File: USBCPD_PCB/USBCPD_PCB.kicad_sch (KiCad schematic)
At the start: 0 parts

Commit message: Added new Parts
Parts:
- added IC1: TMCS1108A3BQDRQ1, SOIC127P600X175-8N, symbol SamacSys_Parts:TMCS1108A3BQDRQ1
- added IC2, IC3: UCC27282QDRQ1, SOIC127P600X175-8N, symbol SamacSys_Parts:UCC27282QDRQ1
- added Q1, Q2, Q3, Q4: SIR584DP-T1-RE3, SIR582DPT1RE3, symbol SamacSys_Parts:SIR584DP-T1-RE3
- added U1: NUCLEO-G474RE, USBC_PD:ST_NUCLEO-G474RE, symbol USBC_PD:NUCLEO-G474RE

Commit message: new components added
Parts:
- added C?: A768MS277M1VLAS022, CAPAE1030X1270N, symbol SamacSys_Parts:A768MS277M1VLAS022
- added C? (x4): GRM32DL8EL475KE07K, CAPC3225X220N, symbol SamacSys_Parts:GRM32DL8EL475KE07K
- added C?: EEE-TP1K391M, EEEFK0J682AM, symbol SamacSys_Parts:EEE-TP1K391M
- added L?: SRP1038WA-150M, SRP1038WA150M, symbol SamacSys_Parts:SRP1038WA-150M
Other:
- moved on the sheet: IC1, IC2, IC3, Q1, Q2, Q3, Q4

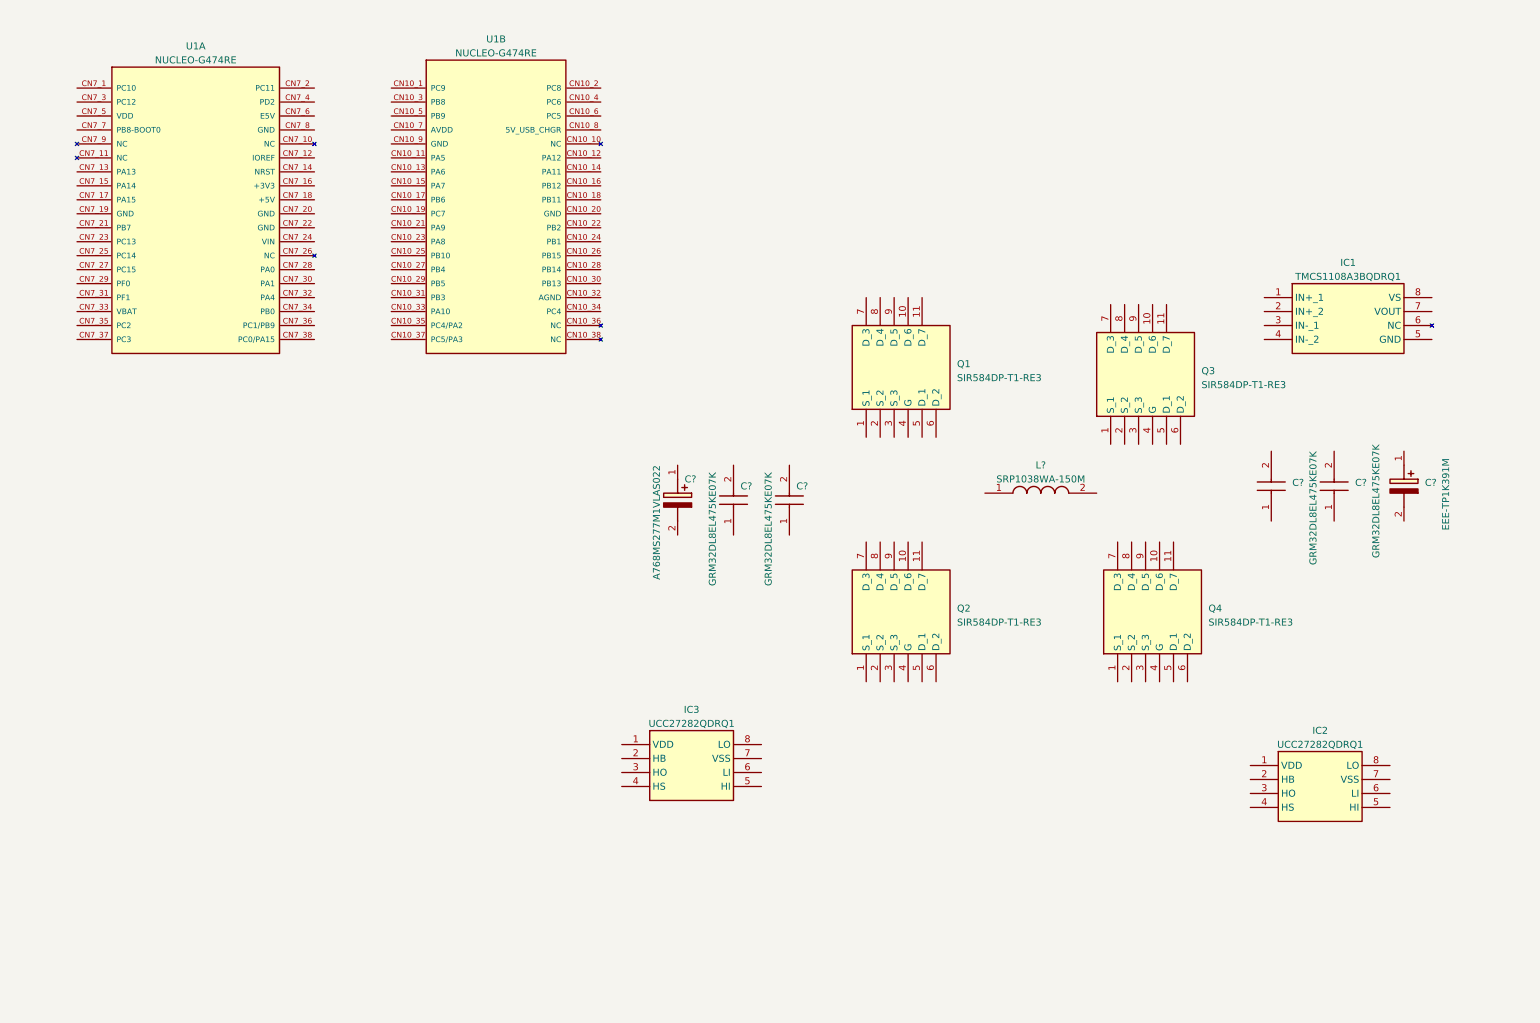
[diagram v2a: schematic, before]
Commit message: added resistors, tvs and voltage control
also wired up first changes
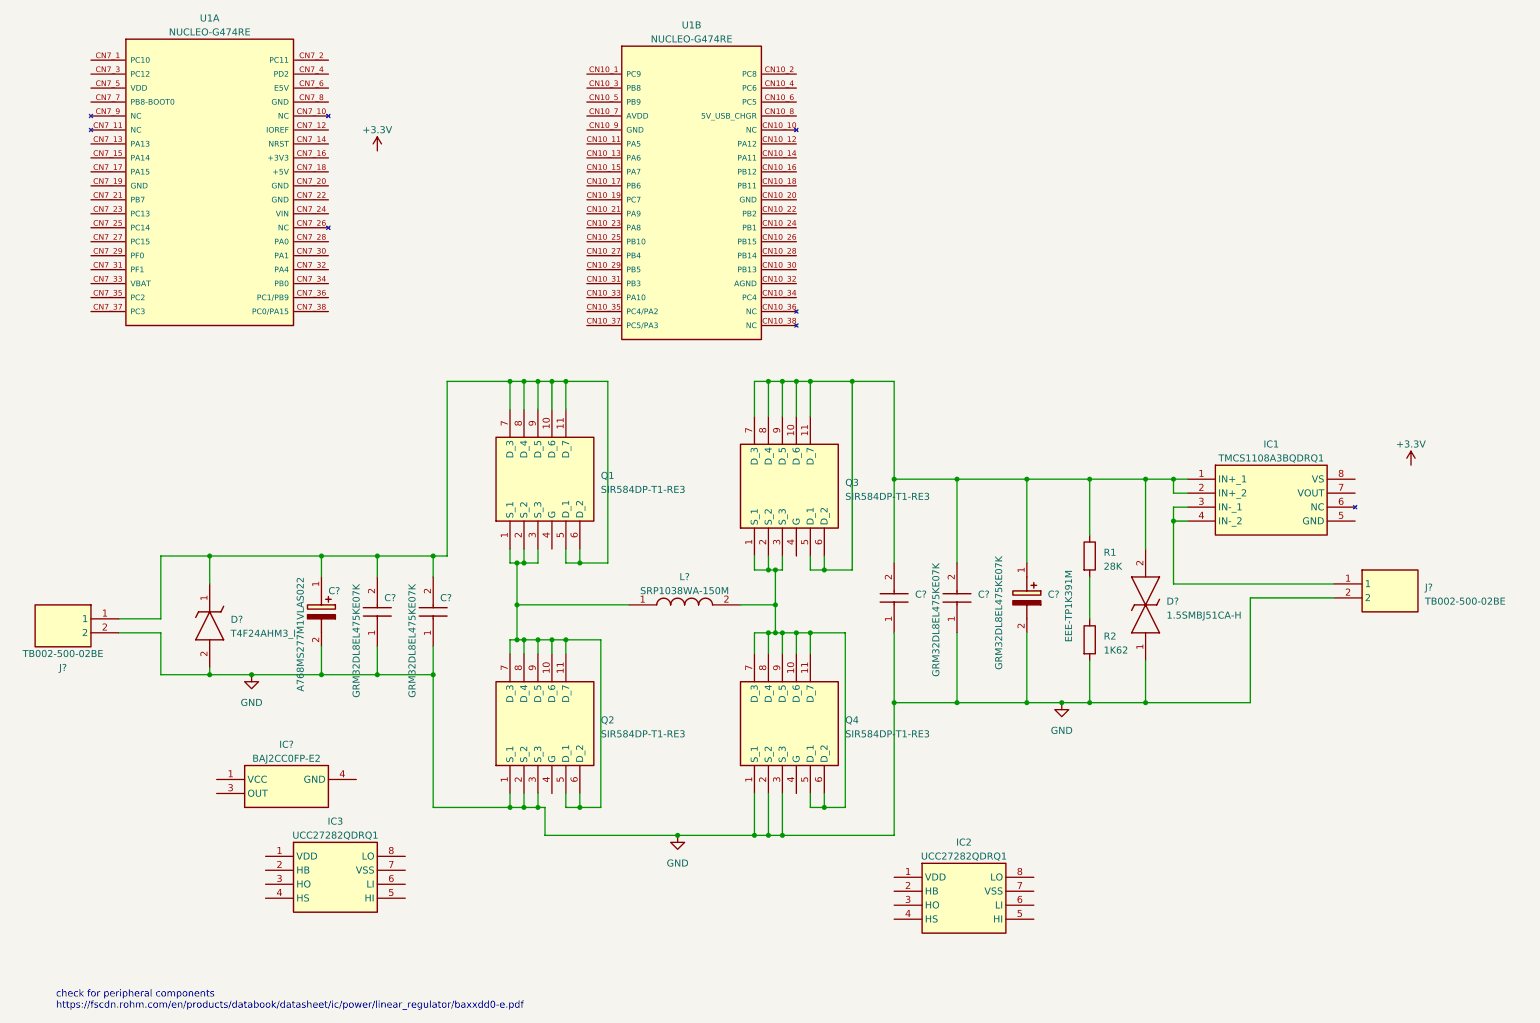
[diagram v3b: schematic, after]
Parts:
- added D?: 1.5SMBJ51CA-H, DIONM5436X244N, symbol SamacSys_Parts:1.5SMBJ51CA-H
- added D?: T4F24AHM3_I, SODFL3718X108N, symbol SamacSys_Parts:T4F24AHM3_I
- added IC?: BAJ2CC0FP-E2, BD750L5FPCE2, symbol SamacSys_Parts:BAJ2CC0FP-E2
- added J? (x2): TB002-500-02BE, TB00250002BE, symbol SamacSys_Parts:TB002-500-02BE
- added R1: 28K, Resistor_SMD:R_0603_1608Metric_Pad0.98x0.95mm_HandSolder, symbol Device:R
- added R2: 1K62, Resistor_SMD:R_0603_1608Metric_Pad0.98x0.95mm_HandSolder, symbol Device:R
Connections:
- net at L?.1: now also Q1.1 (S_1), Q1.2 (S_2), Q1.3 (S_3), Q2.10 (D_6), Q2.11 (D_7), Q2.5 (D_1), Q2.6 (D_2), Q2.7 (D_3), Q2.8 (D_4), Q2.9 (D_5)
- net at L?.2: now also Q3.1 (S_1), Q3.2 (S_2), Q3.3 (S_3), Q4.10 (D_6), Q4.11 (D_7), Q4.5 (D_1), Q4.6 (D_2), Q4.7 (D_3), Q4.8 (D_4), Q4.9 (D_5)
- net GND: now reaches Q2.1 (S_1)
- net GND: now also C?.1, C?.1, C?.1, C?.1, C?.2 (-), C?.2 (-), Q2.2 (S_2), Q2.3 (S_3), Q4.1 (S_1), Q4.2 (S_2), Q4.3 (S_3), D?.1, D?.2 (A), J?.2, J?.2, R2.2
- net at C?.1 (+): now also C?.2, C?.2, Q1.10 (D_6), Q1.11 (D_7), Q1.5 (D_1), Q1.6 (D_2), Q1.7 (D_3), Q1.8 (D_4), Q1.9 (D_5), D?.1 (K), J?.1
- net at Q3.10 (D_6): now also C?.1 (+), C?.2, C?.2, IC1.1 (IN+_1), IC1.2 (IN+_2), Q3.11 (D_7), Q3.5 (D_1), Q3.6 (D_2), Q3.7 (D_3), Q3.8 (D_4), Q3.9 (D_5), D?.2, R1.1
- net at IC1.3 (IN-_1): now also IC1.4 (IN-_2), J?.1
- new net: R1.2, R2.1
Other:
- note added: "check for peripheral components https://fscdn.rohm.com/en/products/databook/datasheet/ic/power/linear_regulator/baxxdd0-e.pdf"
- moved on the sheet: C?, IC1, IC2, IC3, L?, Q1, Q2, Q3, Q4, U1A, U1B

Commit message: added additional components
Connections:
- net +3.3V: now also IC1.8 (VS)
- net GND: now also IC1.5 (GND)
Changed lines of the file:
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@@
+    (stroke (width 0) (type default))
+  )
+  (wire (pts (xy 255.27 105.41) (xy 255.27 102.87))
     (stroke (width 0) (type default))
   )
@@
     (stroke (width 0) (type default))
   )
+  (wire (pts (xy 262.89 95.25) (xy 262.89 92.71))
+    (stroke (width 0) (type default))
+  )
   (wire (pts (xy 214.63 135.89) (xy 204.47 135.89))
     (stroke (width 0) (type default))
@@
     (stroke (width 0) (type default))
   )
+  (wire (pts (xy 255.27 102.87) (xy 252.73 102.87))
+    (stroke (width 0) (type default))
+  )
   (wire (pts (xy 111.76 154.94) (xy 115.57 154.94))
     (stroke (width 0) (type default))
@@
   )
   (wire (pts (xy 146.05 109.22) (xy 146.05 111.76))
+    (stroke (width 0) (type default))
+  )
+  (wire (pts (xy 252.73 95.25) (xy 262.89 95.25))
     (stroke (width 0) (type default))
   )
@@
         )
       )
+    )
+  )
+  (symbol (lib_id "power:GND") (at 255.27 105.41 0) (unit 1)
+    (in_bom yes) (on_board yes) (dnp no) (fields_autoplaced)
+    (property "Reference" "#PWR06" (at 255.27 111.76 0)
+      (effects (font (size 1.27 1.27)) hide)
+    )
+    (property "Value" "GND" (at 255.27 110.49 0)
+      (effects (font (size 1.27 1.27)))
+    )
+    (property "Footprint" "" (at 255.27 105.41 0)
+      (effects (font (size 1.27 1.27)) hide)
+    )
+    (property "Datasheet" "" (at 255.27 105.41 0)
+      (effects (font (size 1.27 1.27)) hide)
+    )
+    (pin "1")
+    (instances
+      (project "USBCPD_PCB"
+        (path "/d348c750-b8a4-4ea0-a85d-ac4257fd8477"
+          (reference "#PWR06") (unit 1)
+        )
+      )

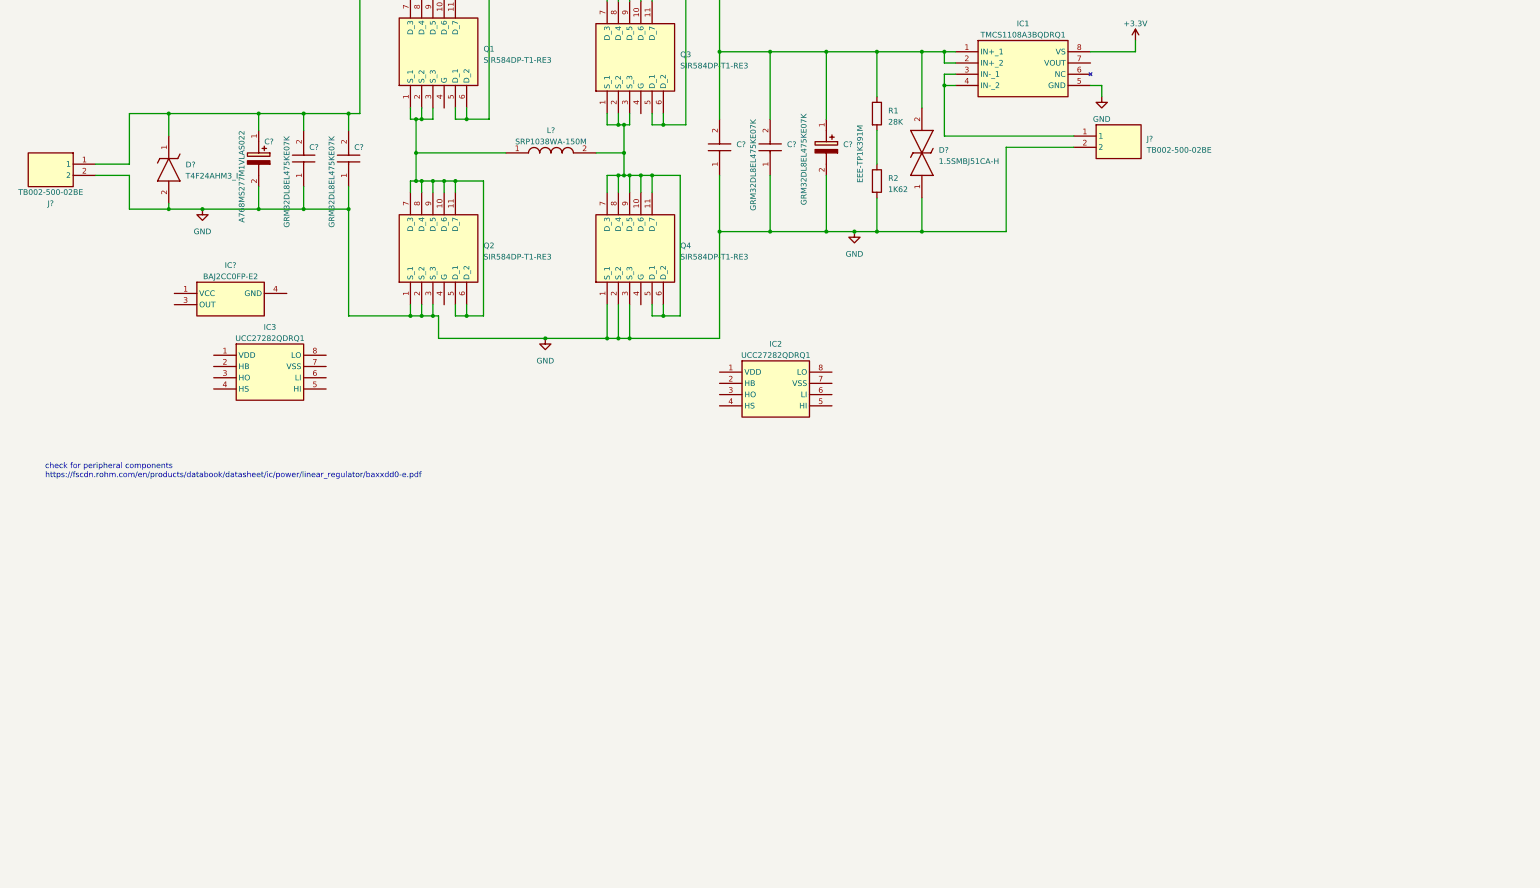
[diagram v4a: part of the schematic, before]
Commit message: Added Gate Driver Circuitry
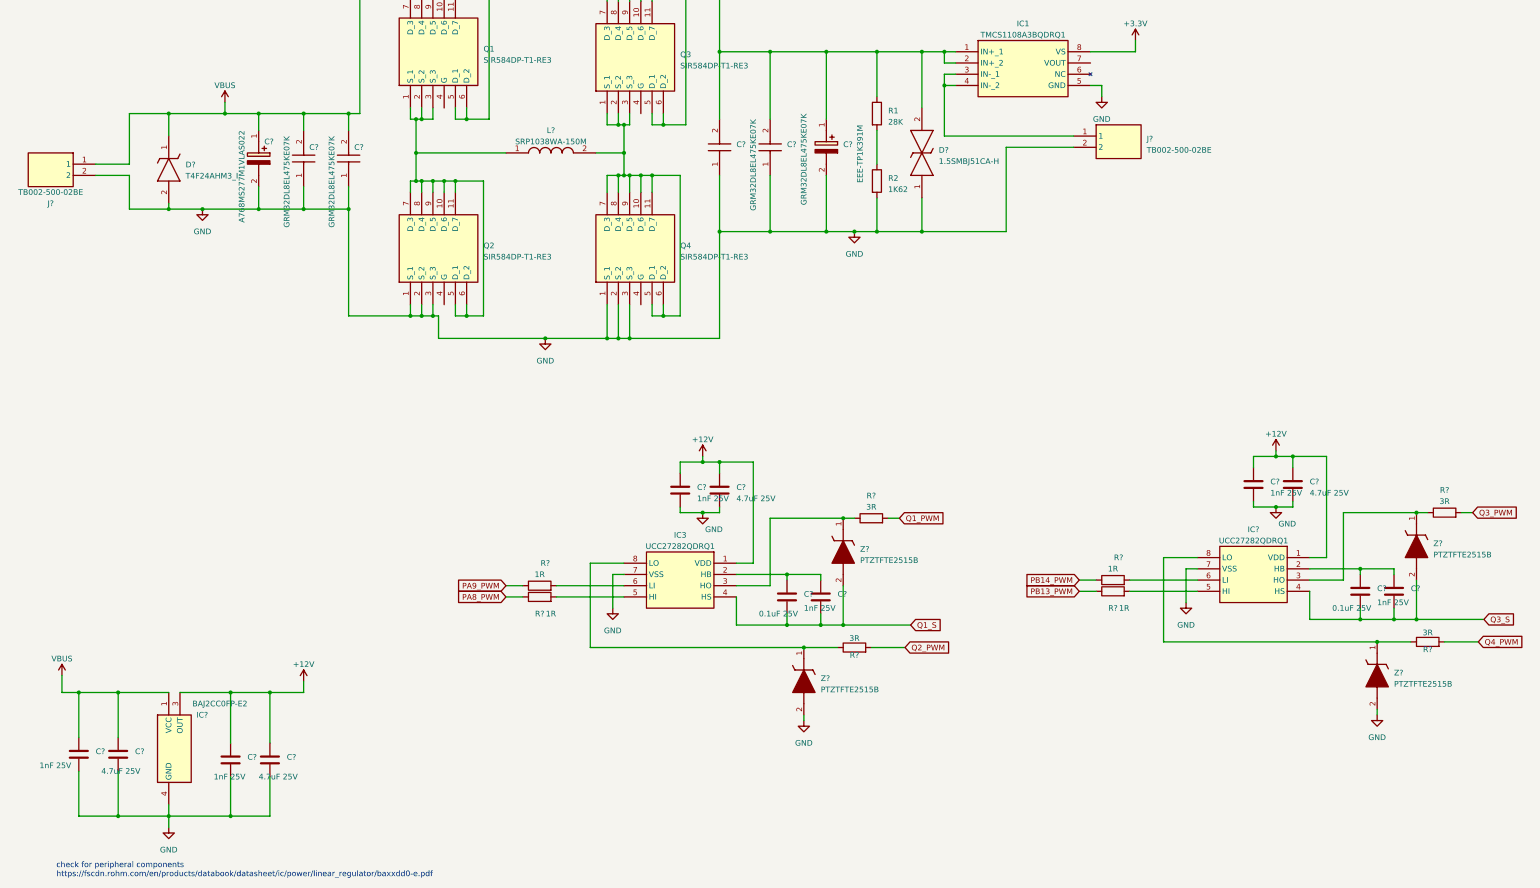
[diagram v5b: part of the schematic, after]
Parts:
- removed IC2: UCC27282QDRQ1, SOIC127P600X175-8N, symbol SamacSys_Parts:UCC27282QDRQ1
- added C? (x4): 4.7uF 25V, Capacitor_SMD:C_0603_1608Metric_Pad1.08x0.95mm_HandSolder, symbol Device:C
- added C? (x6): 1nF 25V, Capacitor_SMD:C_0402_1005Metric_Pad0.74x0.62mm_HandSolder, symbol Device:C
- added C? (x2): 0.1uF 25V, Capacitor_SMD:C_0603_1608Metric_Pad1.08x0.95mm_HandSolder, symbol Device:C
- added IC?: UCC27282QDRQ1, SOIC127P600X175-8N, symbol SamacSys_Parts:UCC27282QDRQ1
- added R? (x4): 1R, Resistor_SMD:R_0603_1608Metric_Pad0.98x0.95mm_HandSolder, symbol Device:R
- added R? (x4): 3R, Resistor_SMD:R_0603_1608Metric_Pad0.98x0.95mm_HandSolder, symbol Device:R
- added Z? (x4): PTZTFTE2515B, PTZTFTE2515B, symbol SamacSys_Parts:PTZTFTE2515B
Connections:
- net GND: now also IC3.7 (VSS), IC?.4 (GND), C?.2, C?.2, C?.2, C?.2, C?.2, C?.2, C?.2, C?.2, IC?.7 (VSS), Z?.2 (A), Z?.2 (A)
- net VBUS: now reaches IC?.1 (VCC)
- net VBUS: now also C?.1 (+), C?.2, C?.2, D?.1 (K), J?.1, Q1.10 (D_6), Q1.11 (D_7), Q1.5 (D_1), Q1.6 (D_2), Q1.7 (D_3), Q1.8 (D_4), Q1.9 (D_5), C?.1, C?.1
- net +12V: now reaches IC?.3 (OUT)
- net +12V: now also IC3.1 (VDD), C?.1, C?.1, C?.1, C?.1, C?.1, C?.1, IC?.1 (VDD)
- net at IC3.2 (HB): now also C?.1, C?.2
- net at IC3.3 (HO): now also R?.1, Z?.1 (K)
- net Q1_S: now reaches IC3.4 (HS)
- net Q1_S: now also C?.1, C?.2, Z?.2 (A)
- net at IC3.5 (HI): now also R?.2
- net at IC3.6 (LI): now also R?.2
- net at IC3.8 (LO): now also R?.1, Z?.1 (K)
- new net: C?.1, C?.2, IC?.2 (HB)
- new net: IC?.3 (HO), R?.1, Z?.1 (K)
- new net: IC?.5 (HI), R?.2
- new net: IC?.6 (LI), R?.2
- new net: IC?.8 (LO), R?.1, Z?.1 (K)
- new net PA8_PWM: R?.1
- new net PA9_PWM: R?.1
- new net PB13_PWM: R?.1
- new net PB14_PWM: R?.1
- new net Q1_PWM: R?.2
- new net Q2_PWM: R?.2
- new net Q3_PWM: R?.2
- new net Q3_S: C?.1, C?.2, IC?.4 (HS), Z?.2 (A)
- new net Q4_PWM: R?.2
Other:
- moved on the sheet: IC3, IC?

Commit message: finished up main schematic
finalized wiring, added leds with resistors, fixed ERC errors
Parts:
- removed C? (x2): 4.7uF 25V, Capacitor_SMD:C_0603_1608Metric_Pad1.08x0.95mm_HandSolder, symbol Device:C
- removed R1: 28K, Resistor_SMD:R_0603_1608Metric_Pad0.98x0.95mm_HandSolder, symbol Device:R
- removed R2: 1K62, Resistor_SMD:R_0603_1608Metric_Pad0.98x0.95mm_HandSolder, symbol Device:R
- added JP1: SolderJumper_2_Bridged, Jumper:SolderJumper-2_P1.3mm_Bridged_RoundedPad1.0x1.5mm, symbol Jumper:SolderJumper_2_Bridged
- added LED1: 150060BS75003, 150060BS75003, symbol SamacSys_Parts:150060BS75003
- added LED2: 150060GS75003, LEDC1608X80N, symbol SamacSys_Parts:150060GS75003
- added LED3: 150060SS75003, 150060SS75003, symbol SamacSys_Parts:150060SS75003
- added R10: 2.8K, Resistor_SMD:R_0603_1608Metric_Pad0.98x0.95mm_HandSolder, symbol Device:R
- added R11, R8: 100R, Resistor_SMD:R_0603_1608Metric_Pad0.98x0.95mm_HandSolder, symbol Device:R
- added R13: 28K, Resistor_SMD:R_0603_1608Metric_Pad0.98x0.95mm_HandSolder, symbol Device:R
- added R14: 1K62, Resistor_SMD:R_0603_1608Metric_Pad0.98x0.95mm_HandSolder, symbol Device:R
- added R5: 1R, Resistor_SMD:R_0603_1608Metric_Pad0.98x0.95mm_HandSolder, symbol Device:R
- added R9: 900R, Resistor_SMD:R_0603_1608Metric_Pad0.98x0.95mm_HandSolder, symbol Device:R
- added S1: EVP-BDCC1A000, EVPBDCC1A000, symbol SamacSys_Parts:EVP-BDCC1A000
- added TP1, TP10, TP2, TP3, TP4, TP5, TP6, TP7, TP8, TP9: TestPoint, TestPoint:TestPoint_THTPad_2.0x2.0mm_Drill1.0mm, symbol Connector:TestPoint
- added unit 5 of U1
- added unit 4 of U1
- added unit 3 of U1
- added unit 6 of U1
- C1: renamed from C?; value 1nF 25V -> 1uF 25V; footprint Capacitor_SMD:C_0402_1005Metric_Pad0.74x0.62mm_HandSolder -> Capacitor_SMD:C_0603_1608Metric_Pad1.08x0.95mm_HandSolder
- C4: renamed from C?; value 1nF 25V -> 0.33uF 25V; footprint Capacitor_SMD:C_0402_1005Metric_Pad0.74x0.62mm_HandSolder -> Capacitor_SMD:C_0603_1608Metric_Pad1.08x0.95mm_HandSolder
- Q1, Q2, Q3, Q4: footprint SIR582DPT1RE3 -> SamacSys_Parts:SIR584DPT1RE3
- gave numbers to parts that had none: 33
- renumbered IC3 to IC2
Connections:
- net +12V: now also TP1.1
- net +3.3V: now also U1.CN7_16 (+3V3)
- net GND: now also U1.CN7_20 (GND), U1.CN7_22 (GND), U1.CN7_8 (GND), JP1.1 (A), LED1.2 (K), LED2.1 (K), LED3.1 (K), R14.2, R8.2
- net PA8_PWM: now also U1.CN10_23 (PA8)
- net PA9_PWM: now also U1.CN10_21 (PA9)
- net PB13_PWM: now also U1.CN10_30 (PB13)
- net PB14_PWM: now also U1.CN10_28 (PB14)
- net Q1_PWM: now also Q1.4 (G)
- net Q1_S: now also L1.1, Q1.1 (S_1), Q1.2 (S_2), Q1.3 (S_3), Q2.10 (D_6), Q2.11 (D_7), Q2.5 (D_1), Q2.6 (D_2), Q2.7 (D_3), Q2.8 (D_4), Q2.9 (D_5), TP3.1
- net Q2_PWM: now also Q2.4 (G)
- net Q3_PWM: now also Q3.4 (G)
- net Q3_S: now also L1.2, Q3.1 (S_1), Q3.2 (S_2), Q3.3 (S_3), Q4.10 (D_6), Q4.11 (D_7), Q4.5 (D_1), Q4.6 (D_2), Q4.7 (D_3), Q4.8 (D_4), Q4.9 (D_5), TP4.1
- net Q4_PWM: now also Q4.4 (G)
- net VBUS: now also R9.1, TP2.1
- net at IC3.3 (HO), R15.1, Z4.1 (K): now also TP10.1
- net at IC3.8 (LO), R12.1, Z3.1 (K): now also TP9.1
- net at IC2.3 (HO), R4.1, Z2.1 (K): now also TP7.1
- net at IC1.3 (IN-_1), IC1.4 (IN-_2), J2.1: now also TP8.1
- net at IC2.8 (LO), R3.1, Z1.1 (K): now also TP6.1
- net PB12_LED: now reaches U1.CN10_16 (PB12)
- net PB12_LED: now also R11.1
- net PB11_BTN: now reaches U1.CN10_18 (PB11)
- net PB11_BTN: now also S1.A1 (COM)
- net PB3_ADC_Iout: now reaches U1.CN10_31 (PB3)
- net PB3_ADC_Iout: now also R5.2
- net PA10_ADC_Vout: now reaches U1.CN10_33 (PA10)
- net PA10_ADC_Vout: now also R13.2, R14.1
- net +BATT: now reaches C6.2, C7.2, C8.1 (+), D2.2, IC1.1 (IN+_1), IC1.2 (IN+_2), Q3.10 (D_6), Q3.11 (D_7), Q3.5 (D_1), Q3.6 (D_2), Q3.7 (D_3), Q3.8 (D_4), Q3.9 (D_5)
- net +BATT: now also R10.1, R13.1, TP5.1
- net at IC1.7 (VOUT): now also R5.1
- new net: JP1.2 (B), R8.1, S1.B1 (NO)
- new net: LED3.2 (A), R11.2
- new net: LED1.1 (A), R9.2
- new net: LED2.2 (A), R10.2
- no-connect marks 0 -> 88
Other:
- note added: "1.9V 20mA Red"
- note added: "3.2V 20mA Blue"
- note added: "3.2V 20mA Green"
- note removed: "check for peripheral components https://fscdn.rohm.com/en/products/databook/datasheet/ic/power/linear_regulator/baxxdd0-e.pdf"
- moved on the sheet: C1, C10, C11, C12, C13, C14, C15, C16, C2, C3, C4, C5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

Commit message: PCB layout, components sorted
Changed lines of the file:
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@@
       (effects (font (size 1.27 1.27)))
     )
-    (property "Value" "1R" (at 210.82 251.46 90)
+    (property "Value" "1R" (at 208.28 254 90)
       (effects (font (size 1.27 1.27)))
     )
